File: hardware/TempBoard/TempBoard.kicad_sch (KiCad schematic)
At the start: 17 parts, among them J1 Conn_01x04, J2 Conn_01x03, U1 BME280

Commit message: pitot board ordered, routing+size finished for temperature board so pull??
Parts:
- removed J1: Conn_01x04, Connector_Molex:Molex_Nano-Fit_105313-xx04_1x04_P2.50mm_Horizontal, symbol Connector_Generic:Conn_01x04
- removed J2: Conn_01x03, Connector_PinHeader_2.54mm:PinHeader_1x03_P2.54mm_Vertical, symbol Connector_Generic:Conn_01x03
- added J2: Conn_01x04, Connector_PinHeader_2.54mm:PinHeader_1x04_P2.54mm_Vertical, symbol Connector_Generic:Conn_01x04
- added J3: Conn_01x05, symbol Connector_Generic:Conn_01x05
- added R5: 0, Resistor_SMD:R_0603_1608Metric_Pad0.98x0.95mm_HandSolder, symbol Device:R
- R2, R3: value 4.6k -> 4.7k
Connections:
- net +3.3V: now also J2.1 (Pin_1), J3.5 (Pin_5)
- net GND: now also J2.4 (Pin_4), J3.1 (Pin_1), J3.2 (Pin_2), R5.1
- net SCL: now also J2.2 (Pin_2), J3.4 (Pin_4)
- net SDA: now also J2.3 (Pin_3), J3.3 (Pin_3)
- net at R4.1, U1.5 (SDO): now also R5.2
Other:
- moved on the sheet: C1, C2, C3, R2, R3, R4, U1

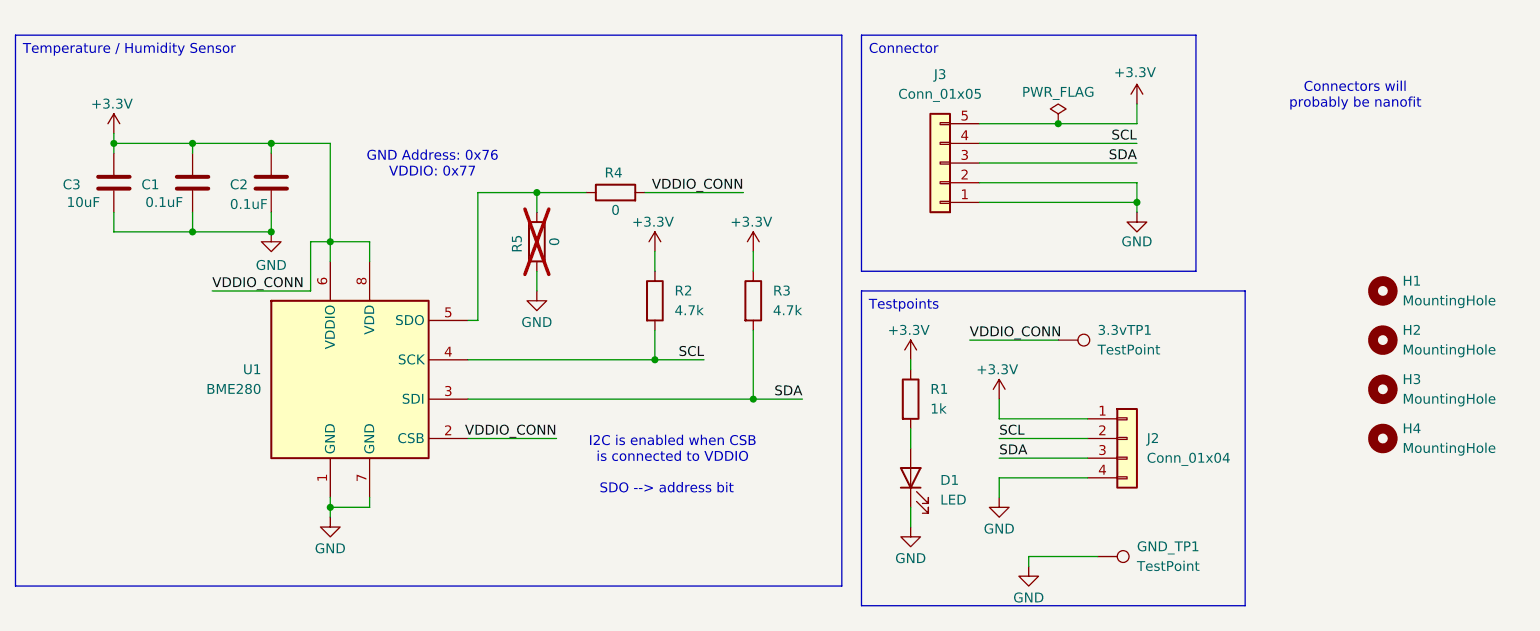
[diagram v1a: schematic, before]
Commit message: finished tempboard silkscreen
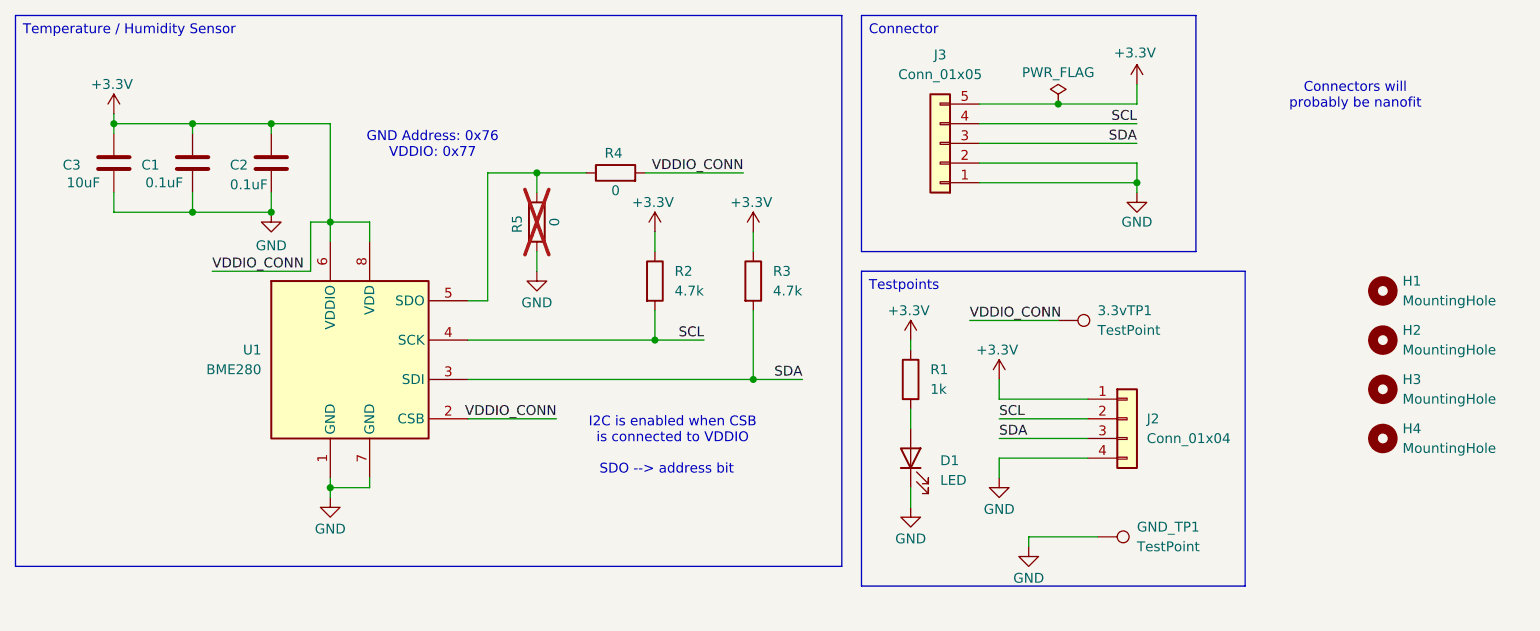
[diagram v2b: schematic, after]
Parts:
- 3.3vTP1: footprint TestPoint:TestPoint_Pad_1.0x1.0mm -> TestPoint:TestPoint_Pad_1.5x1.5mm
- J3: footprint (none) -> Connector_Molex:Molex_Nano-Fit_105313-xx05_1x05_P2.50mm_Horizontal
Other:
- moved on the sheet: 3.3vTP1, C1, C2, C3, D1, GND_TP1, J2, J3, R1, R2, R3, R4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

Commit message: resized temperature board
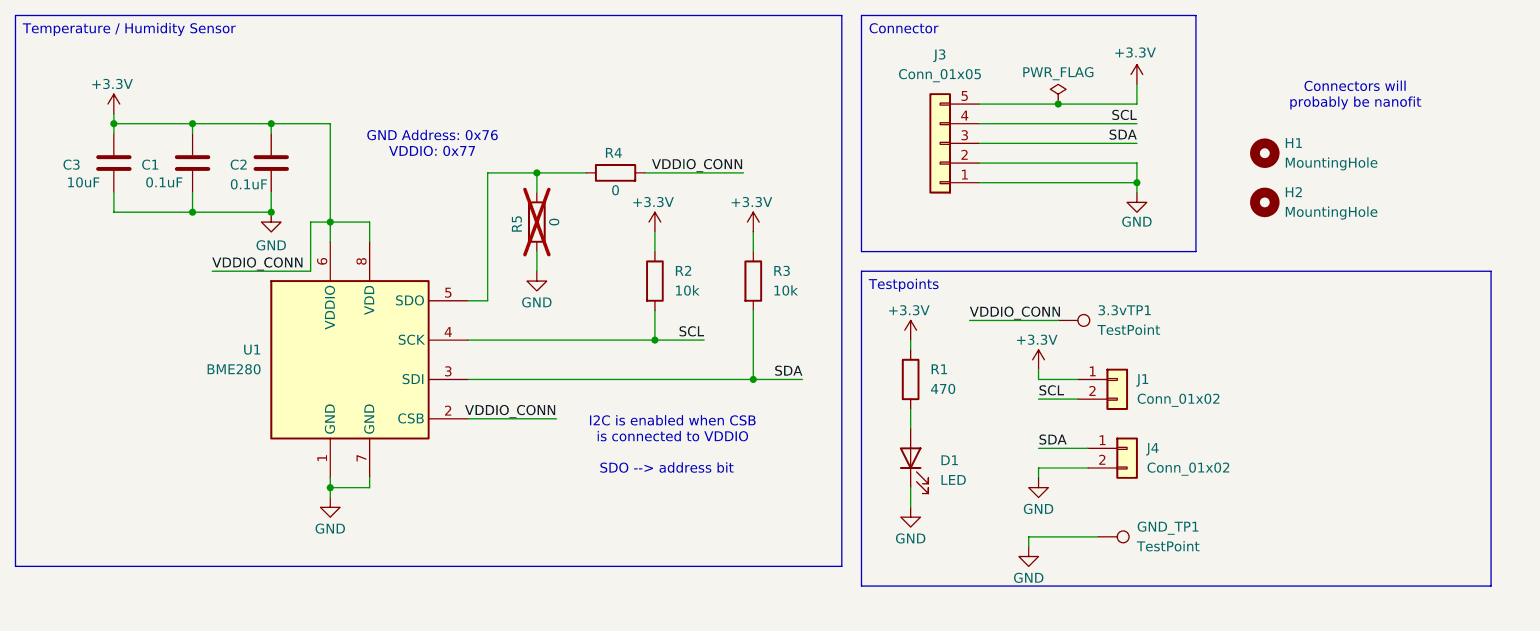
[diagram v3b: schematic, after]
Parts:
- removed H3, H4: MountingHole, MountingHole:MountingHole_3.2mm_M3, symbol Mechanical:MountingHole
- removed J2: Conn_01x04, Connector_PinHeader_2.54mm:PinHeader_1x04_P2.54mm_Vertical, symbol Connector_Generic:Conn_01x04
- added J1, J4: Conn_01x02, Connector_PinHeader_2.54mm:PinHeader_1x02_P2.54mm_Vertical, symbol Connector_Generic:Conn_01x02
- 3.3vTP1: footprint TestPoint:TestPoint_Pad_1.5x1.5mm -> TestPoint:TestPoint_THTPad_1.0x1.0mm_Drill0.5mm
- C3: footprint Capacitor_SMD:C_0603_1608Metric_Pad1.08x0.95mm_HandSolder -> Capacitor_SMD:C_0805_2012Metric_Pad1.18x1.45mm_HandSolder
- GND_TP1: footprint TestPoint:TestPoint_Pad_1.0x1.0mm -> TestPoint:TestPoint_THTPad_1.0x1.0mm_Drill0.5mm
- R1: value 1k -> 470
- R2, R3: value 4.7k -> 10k
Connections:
- net +3.3V: now also J1.1 (Pin_1)
- net GND: now also J4.2 (Pin_2)
- net SCL: now also J1.2 (Pin_2)
- net SDA: now also J4.1 (Pin_1)
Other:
- moved on the sheet: H1, H2
